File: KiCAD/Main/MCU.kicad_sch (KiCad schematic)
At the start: 8 parts, among them U1 STM32H730VBTx

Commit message: post meeting update
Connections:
- net Thermistor_SW1: now reaches U1.1 (PE2)
- net Thermistor_SW2: now reaches U1.2 (PE3)
- net GPS SCL: now reaches U1.59 (PD12)
- net GPS SDA: now reaches U1.60 (PD13)
- net Thermistor_SW4: now reaches U1.97 (PE0)
- net Thermistor_SW3: now reaches U1.98 (PE1)
- net GPS_RX: no longer names the net of U1.22 (PA0)
- net GPS_TX: no longer names the net of U1.23 (PA1)

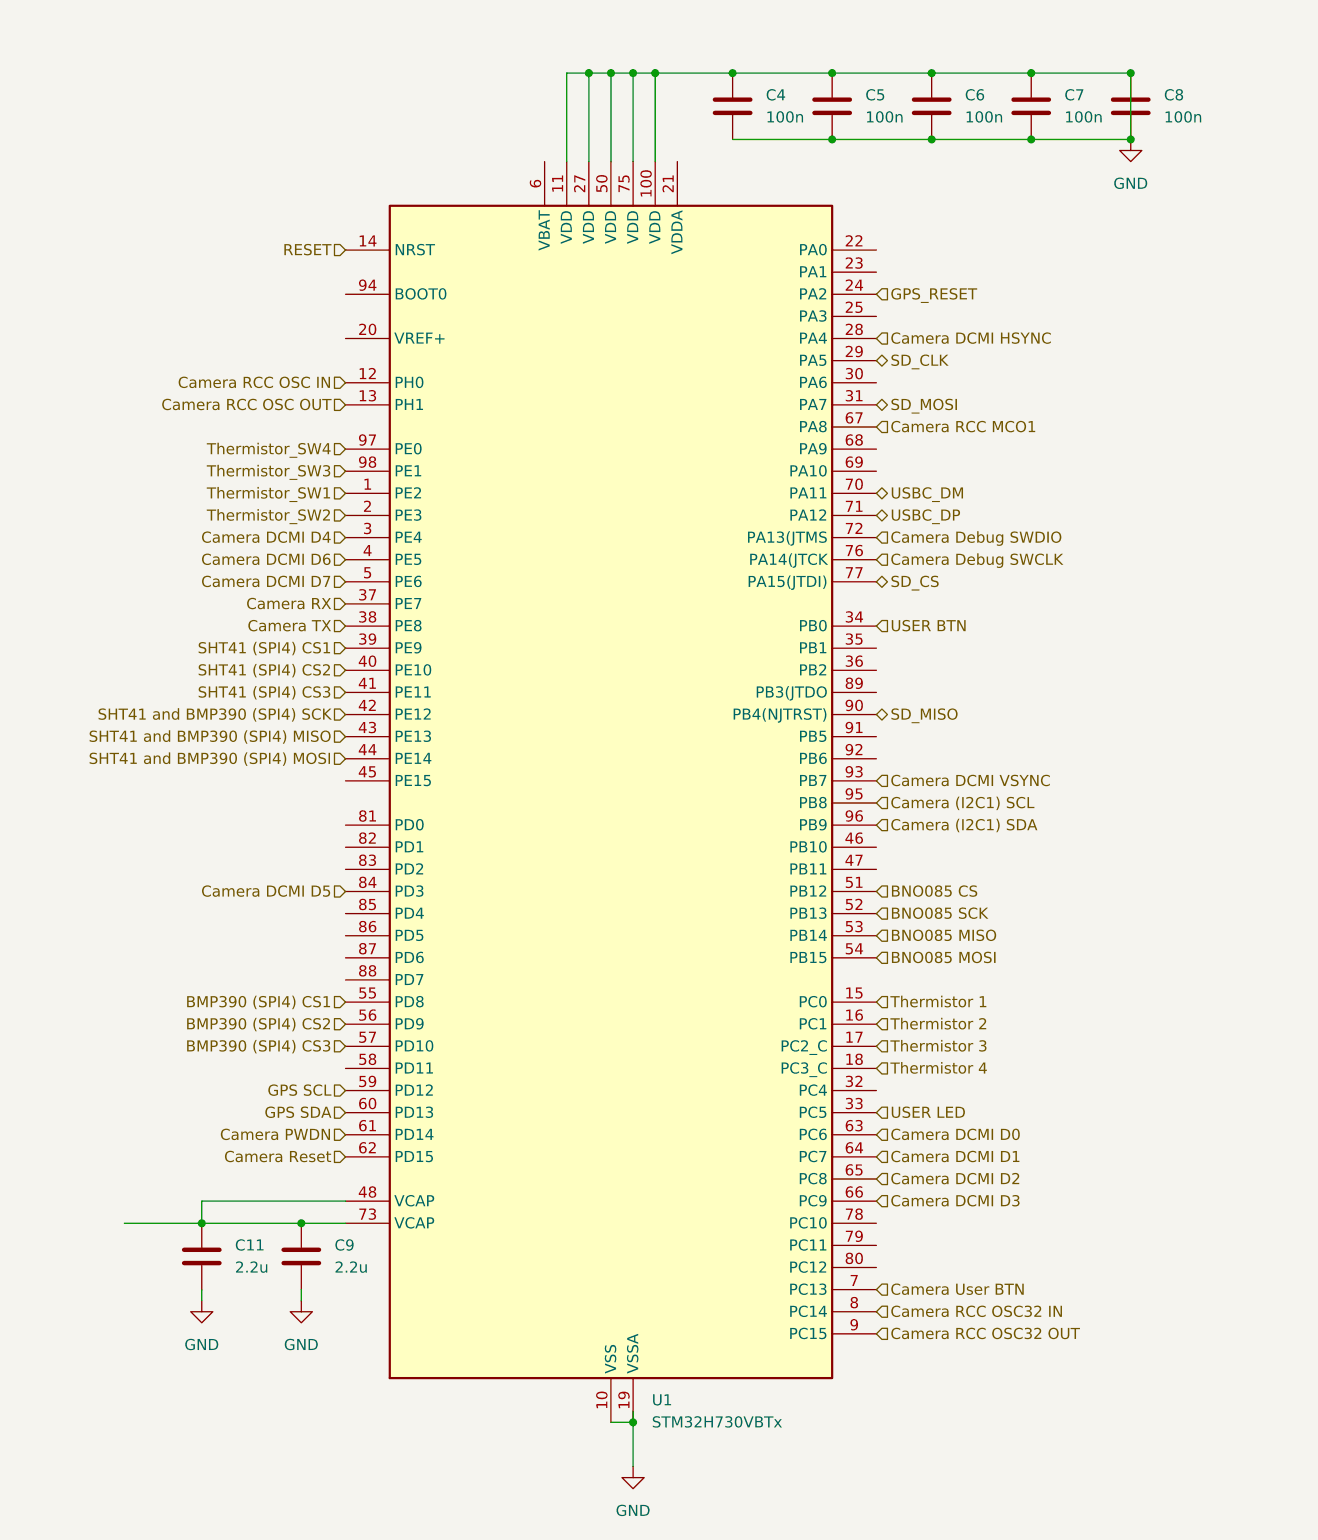
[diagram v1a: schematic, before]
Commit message: Remove thermocouples due to complexity and focus switch
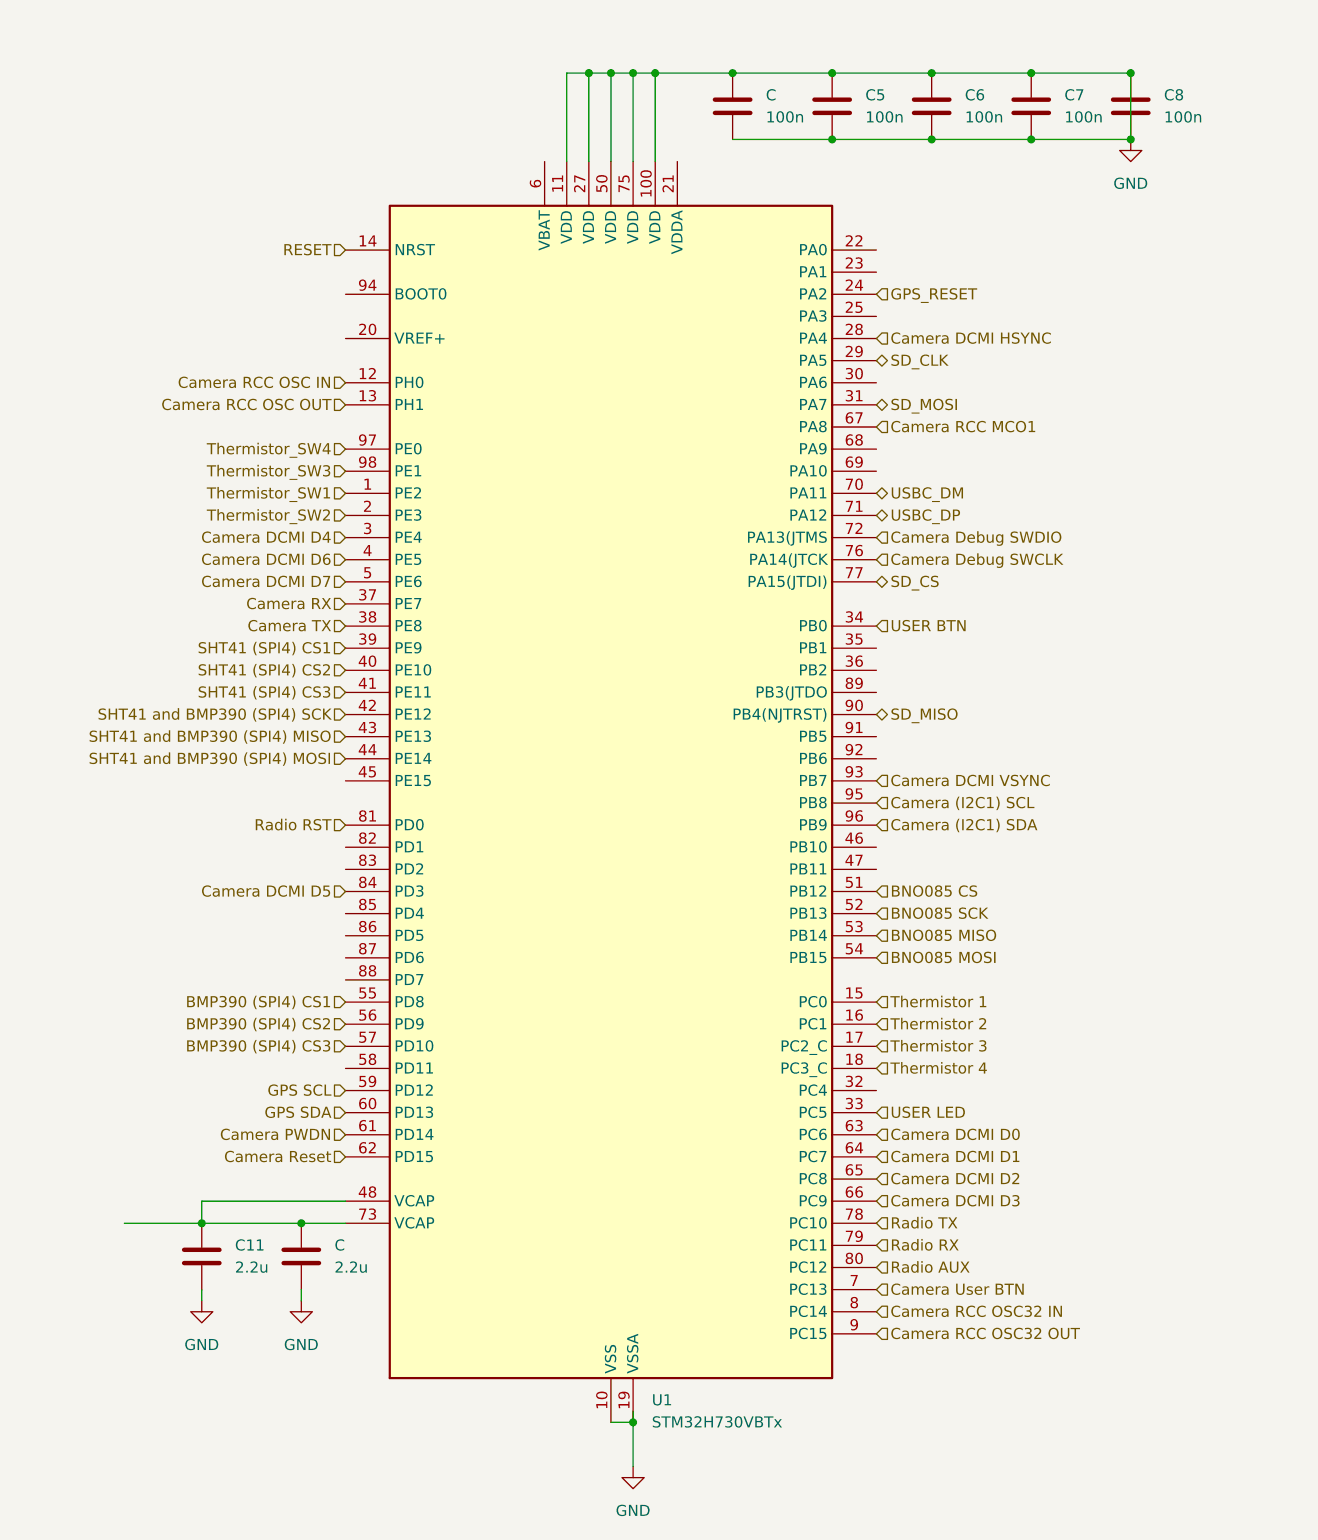
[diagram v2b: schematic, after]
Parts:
- renumbered C4 to C, C9 to C
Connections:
- net Radio TX: now reaches U1.78 (PC10)
- net Radio RX: now reaches U1.79 (PC11)
- net Radio AUX: now reaches U1.80 (PC12)
- net Radio RST: now reaches U1.81 (PD0)

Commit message: prep for merge
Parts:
- added C9: 100n, symbol Device:C
- renumbered C to C?
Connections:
- net GND: now also C11.1, C?.1, U1.48 (VCAP), U1.73 (VCAP); no longer C5.1, C5.2, C6.1, C6.2, C7.1, C7.2, C8.1, C8.2, C?.1, C?.2, U1.100 (VDD), U1.11 (VDD), U1.27 (VDD), U1.50 (VDD), U1.75 (VDD)
- net at U1.21 (VDDA): now also C5.1, C6.1, C7.1, C8.1, C?.1, U1.100 (VDD), U1.11 (VDD), U1.27 (VDD), U1.50 (VDD), U1.75 (VDD), C9.1
- net +3V3: now reaches U1.6 (VBAT)
- net +3V3: now also C5.2, C6.2, C7.2, C8.2, C?.2, C9.2
- net Thermistor 1 renamed Drogue_Main_Pyro
- net Thermistor 2 renamed Drogue Backup Pyro
- net Thermistor 3: no longer names the net of U1.17 (PC2_C)
- net Thermistor 4: no longer names the net of U1.18 (PC3_C)
- net Thermistor_SW1: no longer names the net of U1.1 (PE2)
- net Thermistor_SW2: no longer names the net of U1.2 (PE3)
- net Thermistor_SW3: no longer names the net of U1.98 (PE1)
- net Thermistor_SW4: no longer names the net of U1.97 (PE0)
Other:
- moved on the sheet: C8
